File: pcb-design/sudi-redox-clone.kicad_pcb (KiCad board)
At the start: 2 copper layers, 141.8 x 99.4 mm, 143 parts, among them J1 SIDE_CON, J10 ARM_JTAG, J2 0.91 OLED, J5 SIDE_CON, J6 USB_A, J7 ARMJTAG, J8 BatCon, J9 AVR-ISP-6, K1 KEYSW, K10 KEYSW, K11 KEYSW, K12 KEYSW, K13 KEYSW, K14 KEYSW, K15 KEYSW, K16 KEYSW, K17 KEYSW, K18 KEYSW, K2 KEYSW, K3 KEYSW, K4 KEYSW, K5 KEYSW, K6 KEYSW, K7 KEYSW, K8 KEYSW, K9 KEYSW, P1 USB_C_Plug_USB2.0, SW1 RST, SW2 RCV_RST, U1 AMS1117-3.3, U2 ATmega8U2-A, U3 nRF51x22-QFxx, U4 AMS1117-3.3, U5 CH340C, U6 TP4056, U7 nRF52832-QFxx, U8 MCP23017_SS, Y3 16MHz, Y4 8MHz, Y5 32MHz

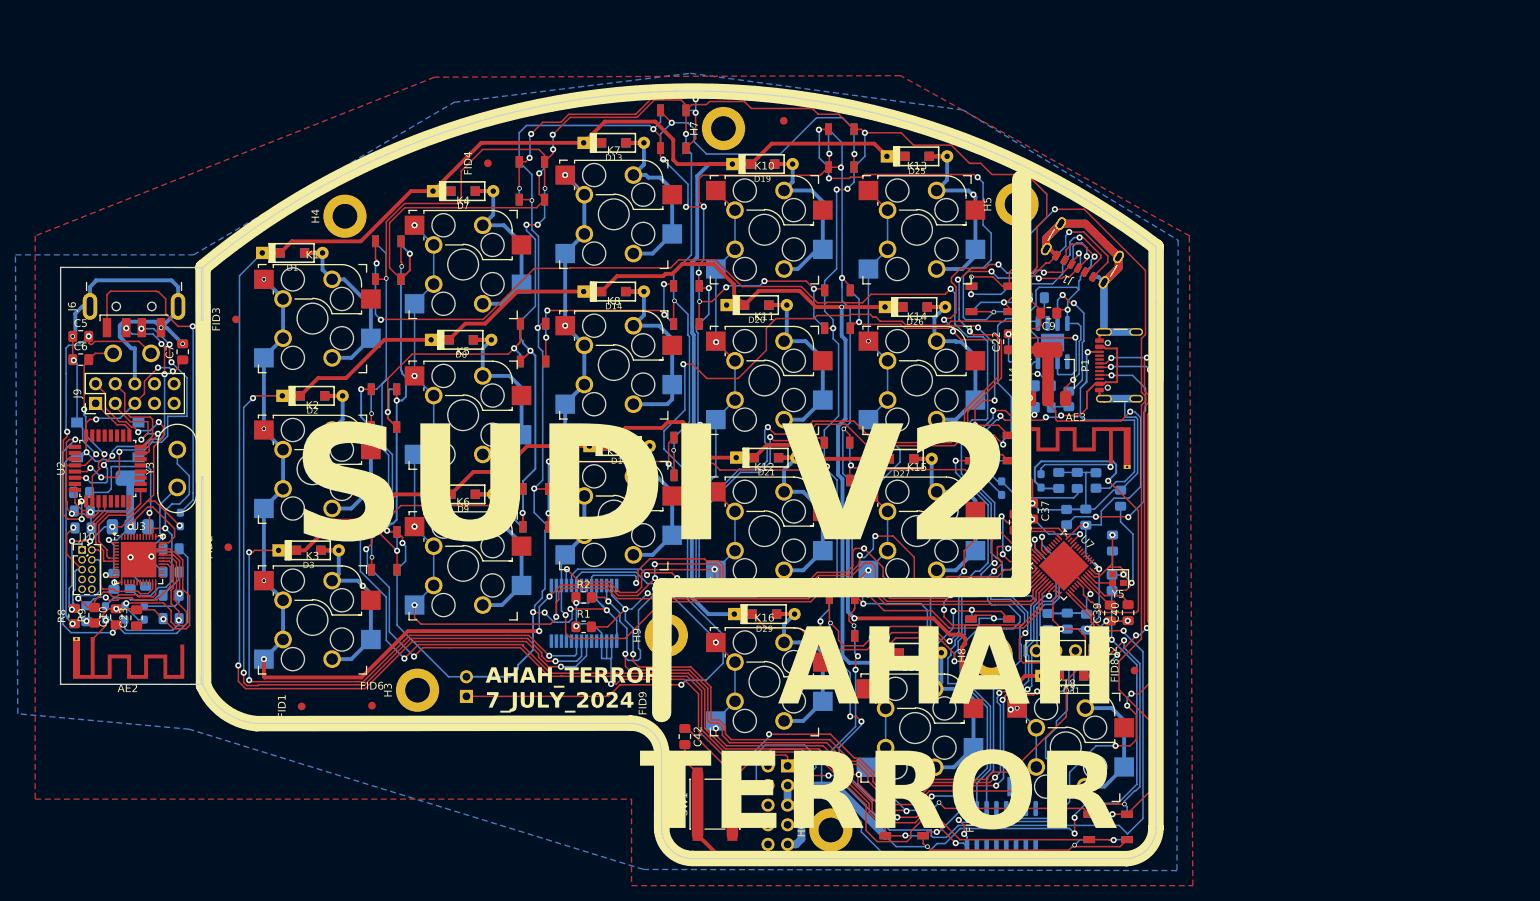
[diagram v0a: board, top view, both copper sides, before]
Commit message: [11-01-1954] add test point into NRF
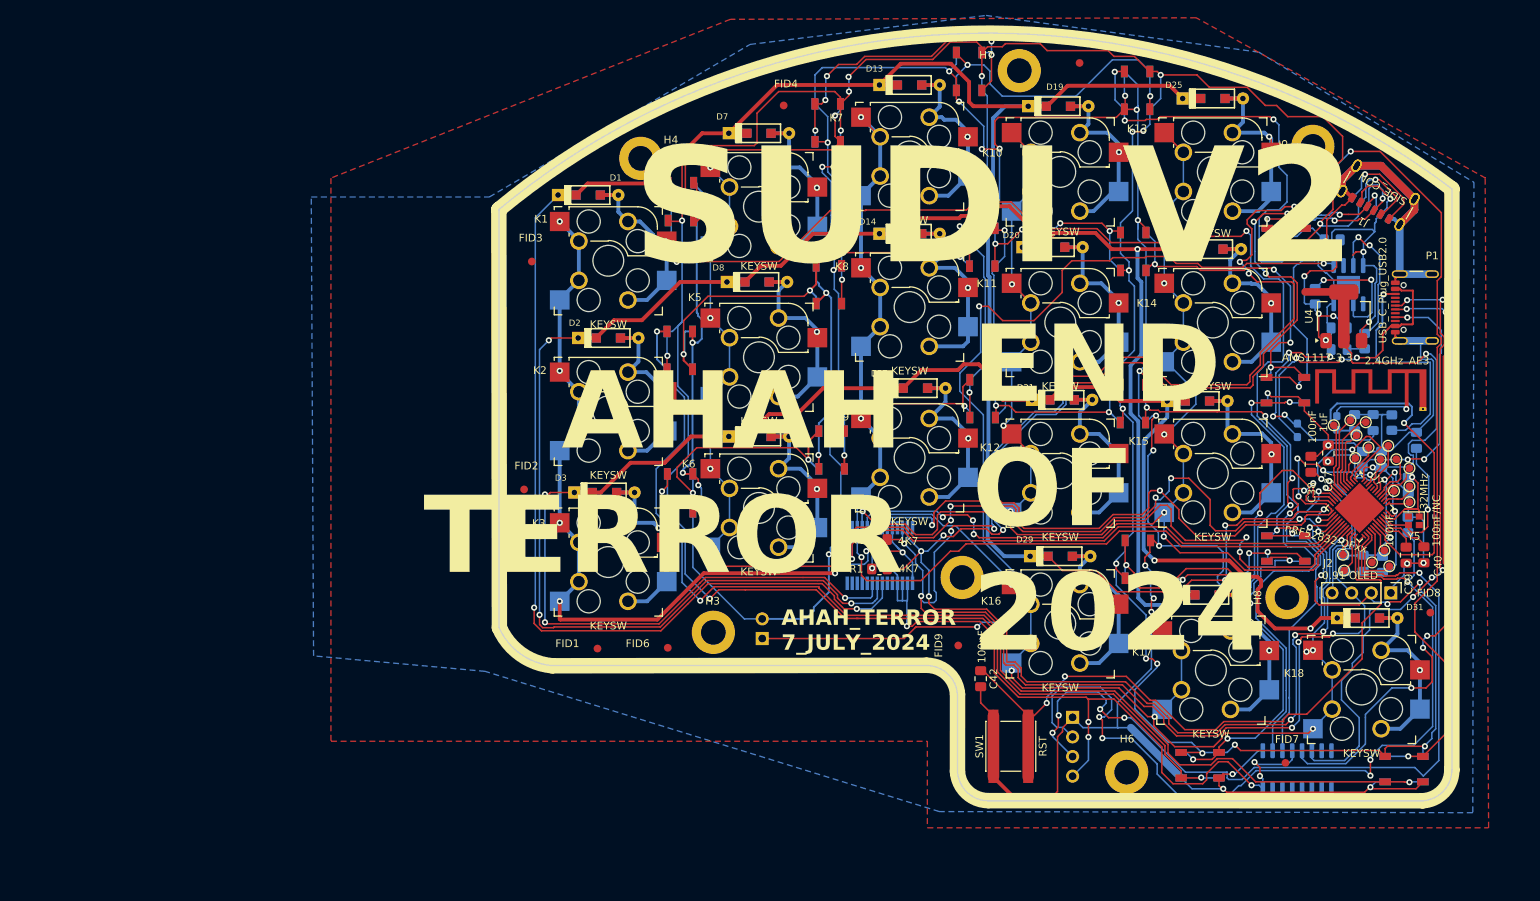
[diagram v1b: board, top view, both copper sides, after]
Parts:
- removed AE2: 2.4GHz, RF_Antenna:Texas_SWRA117D_2.4GHz_Left
- removed C10: 1uF, Capacitor_SMD:C_0805_2012Metric_Pad1.18x1.45mm_HandSolder
- removed C22, C9: 10uF/5V, Capacitor_SMD:C_0805_2012Metric_Pad1.18x1.45mm_HandSolder
- removed C23, C31, C32, C33, C7: 100nF, Capacitor_SMD:C_0805_2012Metric_Pad1.18x1.45mm_HandSolder
- removed C24: 1.5p, Capacitor_SMD:C_0805_2012Metric_Pad1.18x1.45mm_HandSolder
- removed C25: 1pF, Capacitor_SMD:C_0805_2012Metric_Pad1.18x1.45mm_HandSolder
- removed C26: 2.2pF, Capacitor_SMD:C_0805_2012Metric_Pad1.18x1.45mm_HandSolder
- removed C27: 2.2nF, Capacitor_SMD:C_0805_2012Metric_Pad1.18x1.45mm_HandSolder
- removed C28, C29: 12pF, Capacitor_SMD:C_0805_2012Metric_Pad1.18x1.45mm_HandSolder
- removed C30: 47nF, Capacitor_SMD:C_0805_2012Metric_Pad1.18x1.45mm_HandSolder
- removed C34: 1nF, Capacitor_SMD:C_0805_2012Metric_Pad1.18x1.45mm_HandSolder
- removed C5, C6: 22pF, Capacitor_SMD:C_0805_2012Metric_Pad1.18x1.45mm_HandSolder
- removed FB2: 60R@100Mhz, Inductor_SMD:L_0603_1608Metric_Pad1.05x0.95mm_HandSolder
- removed J10: ARM_JTAG, Connector_PinHeader_1.27mm:PinHeader_2x05_P1.27mm_Vertical
- removed J6: USB_A, Connector_USB:USB_A_CNCTech_1001-011-01101_Horizontal
- removed J7: ARMJTAG, Connector_PinHeader_2.54mm:PinHeader_2x05_P2.54mm_Horizontal
- removed J9: AVR-ISP-6, Connector_PinHeader_2.54mm:PinHeader_2x05_P2.54mm_Vertical
- removed L4: 3.3nH, Inductor_SMD:L_0603_1608Metric_Pad1.05x0.95mm_HandSolder
- removed L5: 10nH, Inductor_SMD:L_0603_1608Metric_Pad1.05x0.95mm_HandSolder
- removed L6: 4.7nH, Inductor_SMD:L_0603_1608Metric_Pad1.05x0.95mm_HandSolder
- removed R8, R9: 1K, Resistor_SMD:R_0805_2012Metric_Pad1.20x1.40mm_HandSolder
- removed SW2: RCV_RST, Button_Switch_SMD:SW_Push_1P1T_NO_6x6mm_H9.5mm
- removed U1: AMS1117-3.3, Package_TO_SOT_SMD:SOT-223-3_TabPin2
- removed U2: ATmega8U2-A, Package_QFP:TQFP-32_7x7mm_P0.8mm
- removed U3: nRF51x22-QFxx, Package_DFN_QFN:QFN-48-1EP_6x6mm_P0.4mm_EP4.6x4.6mm
- removed Y3: 16MHz, Crystal:Crystal_HC50_Vertical
- removed Y4: 8MHz, Crystal:Crystal_HC50_Vertical
- added J3: SWD_JLINK, Connector_PinHeader_2.54mm:PinHeader_1x04_P2.54mm_Horizontal, B.Cu at (182.7, 134.2)
- added TP1: TestPoint, TestPoint:TestPoint_Pad_D1.0mm, F.Cu at (217.7, 113.2)
- added TP10: TestPoint, TestPoint:TestPoint_Pad_D1.0mm, F.Cu at (224.6, 100.8)
- added TP11: TestPoint, TestPoint:TestPoint_Pad_D1.0mm, F.Cu at (223.5, 99.1)
- added TP12: TestPoint, TestPoint:TestPoint_Pad_D1.0mm, F.Cu at (222.5, 100.8)
- added TP14: TestPoint, TestPoint:TestPoint_Pad_D1.0mm, F.Cu at (219.3, 100.7)
- added TP15: TestPoint, TestPoint:TestPoint_Pad_D1.0mm, F.Cu at (219.4, 97.7)
- added TP17: TestPoint, TestPoint:TestPoint_Pad_D1.0mm, F.Cu at (218.6, 95.8)
- added TP18: TestPoint, TestPoint:TestPoint_Pad_D1.0mm, F.Cu at (216.5, 96.4)
- added TP2: TestPoint, TestPoint:TestPoint_Pad_D1.0mm, F.Cu at (223.7, 114.7)
- added TP3: TestPoint, TestPoint:TestPoint_Pad_D1.0mm, F.Cu at (217.8, 115.2)
- added TP4: TestPoint, TestPoint:TestPoint_Pad_D1.0mm, F.Cu at (221.4, 114.2)
- added TP5: TestPoint, TestPoint:TestPoint_Pad_D1.0mm, F.Cu at (223.0, 112.6)
- added TP6: TestPoint, TestPoint:TestPoint_Pad_D1.0mm, F.Cu at (226.3, 106.4)
- added TP7: TestPoint, TestPoint:TestPoint_Pad_D1.0mm, F.Cu at (226.3, 104.3)
- added TP8: TestPoint, TestPoint:TestPoint_Pad_D1.0mm, F.Cu at (224.3, 104.9)
- added TP9: TestPoint, TestPoint:TestPoint_Pad_D1.0mm, F.Cu at (226.3, 102.0)
- added TPe: TestPoint, TestPoint:TestPoint_Pad_D1.0mm, F.Cu at (220.6, 96.0)
- added TPe: TestPoint, TestPoint:TestPoint_Pad_D1.0mm, F.Cu at (221.0, 99.3)
- H9: moved to B.Cu
- moved C39 39.0 mm to (225.9, 113.2)
- moved FID8 39.0 mm to (229.0, 120.7)
- moved J1 39.0 mm to (222.8, 65.7)
- moved J5 39.0 mm to (222.8, 65.7)
- moved Y5 39.0 mm to (226.9, 108.8)
- moved D10 39.0 mm to (171.0, 73.4)
- moved D12 39.0 mm to (210.2, 91.9)
- moved D23 39.0 mm to (190.5, 93.6)
- moved FID7 39.0 mm to (210.2, 140.1)
- moved R6 39.0 mm to (220.5, 85.5)
- moved U6 39.0 mm to (218.4, 78.2)
- moved D5 39.0 mm to (131.8, 86.7)
- moved D13 39.0 mm to (161.6, 52.4)
- moved D14 39.0 mm to (161.6, 71.6)
- moved D15 39.0 mm to (162.3, 91.6)
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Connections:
- U7 pad 2: unconnected-(U7-P0.00/XL1-Pad2) -> /P0.00/XL1
- U7 pad 22: unconnected-(U7-P0.19-Pad22) -> /P0.19
- U7 pad 23: unconnected-(U7-P0.20-Pad23) -> /P0.20
- U7 pad 27: unconnected-(U7-P0.22-Pad27) -> /P0.22
- U7 pad 28: unconnected-(U7-P0.23-Pad28) -> /P0.23
- U7 pad 29: unconnected-(U7-P0.24-Pad29) -> /P0.24
- U7 pad 3: unconnected-(U7-P0.01/XL2-Pad3) -> /P0.01/XL2
- U7 pad 37: unconnected-(U7-P0.25-Pad37) -> /P0.25
- U7 pad 38: unconnected-(U7-P0.26-Pad38) -> /P0.26
- U7 pad 39: unconnected-(U7-P0.27-Pad39) -> /P0.27
- U7 pad 4: unconnected-(U7-P0.02/AIN0-Pad4) -> /P0.02/AIN0
- U7 pad 40: unconnected-(U7-P0.28/AIN4-Pad40) -> /P0.28/AIN4
- U7 pad 41: unconnected-(U7-P0.29/AIN5-Pad41) -> /P0.29/AIN5
- U7 pad 42: unconnected-(U7-P0.30/AIN6-Pad42) -> /P0.30/AIN6
- U7 pad 43: unconnected-(U7-P0.31/AIN7-Pad43) -> /P0.31/AIN7
- U7 pad 5: unconnected-(U7-P0.03/AIN1-Pad5) -> /P0.03/AIN1
- U7 pad 6: unconnected-(U7-P0.04/AIN2-Pad6) -> /P0.04/AIN2
- U7 pad 7: unconnected-(U7-P0.05/AIN3-Pad7) -> /P0.05/AIN3
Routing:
- net GND: track 837.4 -> 705.3 mm, vias 58 -> 47
- net /Receiver/RCV_RST: track 53.7 -> 0.00 mm, vias 5 -> 0
- net +5V: track 135.7 -> 84.9 mm, vias 14 -> 7
- net Net-(J6-VBUS): track 43.4 -> 0.00 mm, vias 1 -> 0
- net Net-(U2-XTAL1): track 41.1 -> 0.00 mm, vias 4 -> 0
- net Net-(U2-UCAP): track 37.2 -> 0.00 mm, vias 2 -> 0
- net Net-(J6-D+): track 36.5 -> 0.00 mm, vias 6 -> 0
- net Net-(J6-D-): track 34.2 -> 0.00 mm, vias 6 -> 0
- net +3.3V: track 311.0 -> 278.5 mm, vias 20 -> 16
- net Net-(U3-XC2): track 29.1 -> 0.00 mm, vias 1 -> 0
- net Net-(AE2-A): track 25.2 -> 0.00 mm, vias 1 -> 0
- net Net-(U3-ANT1): track 24.4 -> 0.00 mm, vias 1 -> 0
- net Net-(U2-PC0/XTAL2): track 24.0 -> 0.00 mm, vias 2 -> 0
- net Net-(J10-SWCLK): track 22.2 -> 0.00 mm, vias 1 -> 0
- net Net-(U3-DEC1): track 19.9 -> 0.00 mm, vias 1 -> 0
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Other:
- board size 141.8 x 99.4 mm -> 123.4 x 99.4 mm
- board text added: "9 11 2023 7 7 2024 1 11 2024"
- board text added: "END OF 2024"
- board text added: "FINISHED AT 1 NOV 2024"
- board text removed: "9 November 2023 7 Juli 2024"

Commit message: [16-11-1807] change chargin mechanism
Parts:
- removed AE3: 2.4GHz, RF_Antenna:Texas_SWRA117D_2.4GHz_Left
- removed C41: 0.8pF, Capacitor_SMD:C_0805_2012Metric_Pad1.18x1.45mm_HandSolder
- removed C42: 100nF, Capacitor_SMD:C_0805_2012Metric_Pad1.18x1.45mm_HandSolder
- removed D43, D44, D45, D46, D47, D48: WS2812B, CustomWS2185BFootPrint:LED_WS2812B_PLCC4_5.0x5.0mm_P3.2mm
- removed H8, H9: MountingHole_Pad, MountingHole:MountingHole_3.2mm_M3_DIN965_Pad
- removed J8: BatCon, Connector_PinHeader_2.54mm:PinHeader_1x02_P2.54mm_Horizontal
- removed L7: 3.9nH, Inductor_SMD:L_0603_1608Metric_Pad1.05x0.95mm_HandSolder
- removed TPe (x2): TestPoint, TestPoint:TestPoint_Pad_D1.0mm
- removed Y5: 32MHz, Crystal:Crystal_SMD_2016-4Pin_2.0x1.6mm
- added AE1: 2.4GHz, RF_Antenna:Texas_SWRA117D_2.4GHz_Left, F.Cu at (219.8, 88.7)
- added C11: 0.1uF, Capacitor_SMD:C_0805_2012Metric_Pad1.18x1.45mm_HandSolder, B.Cu at (161.3, 120.2)
- added C12: 10uF, Capacitor_SMD:C_0805_2012Metric_Pad1.18x1.45mm_HandSolder, B.Cu at (170.4, 122.2)
- added C13: 10uF, Capacitor_SMD:C_0805_2012Metric_Pad1.18x1.45mm_HandSolder, B.Cu at (170.4, 124.7)
- added C14: 10uF, Capacitor_SMD:C_0805_2012Metric_Pad1.18x1.45mm_HandSolder, B.Cu at (130.4, 125.4)
- added C15: 0.1uF, Capacitor_SMD:C_0805_2012Metric_Pad1.18x1.45mm_HandSolder, B.Cu at (130.4, 121.0)
- added C16: 10uF, Capacitor_SMD:C_0805_2012Metric_Pad1.18x1.45mm_HandSolder, B.Cu at (143.7, 116.5)
- added C17: 10uF, Capacitor_SMD:C_0805_2012Metric_Pad1.18x1.45mm_HandSolder, B.Cu at (143.7, 118.9)
- added C18: 12pF, Capacitor_SMD:C_0805_2012Metric_Pad1.18x1.45mm_HandSolder, F.Cu at (228.8, 94.5)
- added C21: 0.8pF, Capacitor_SMD:C_0805_2012Metric_Pad1.18x1.45mm_HandSolder, F.Cu at (228.1, 91.3)
- added D32: red, LED_SMD:LED_0805_2012Metric_Pad1.15x1.40mm_HandSolder, F.Cu at (149.6, 118.9)
- added D33: 1N4148, canadian_footprints:D_SOD123_axial-dual, F.Cu at (181.9, 112.8)
- added D34: 1N4148, canadian_footprints:D_SOD123_axial-dual, F.Cu at (199.8, 119.0)
- added D35: 1N4148, canadian_footprints:D_SOD123_axial-dual, F.Cu at (220.1, 139.7)
- added D36: WS2812B, LED_SMD:LED_WS2812B-2020_PLCC4_2.0x2.0mm, F.Cu at (151.5, 99.7)
- added D37: WS2812B, LED_SMD:LED_WS2812B-2020_PLCC4_2.0x2.0mm, F.Cu at (189.8, 93.2)
- added D38: WS2812B, LED_SMD:LED_WS2812B-2020_PLCC4_2.0x2.0mm, F.Cu at (228.4, 140.5)
- added H1: MountingHole_Pad, MountingHole:MountingHole_3.2mm_M3_DIN965_Pad, F.Cu at (210.6, 118.8)
- added H2: MountingHole_Pad, MountingHole:MountingHole_3.2mm_M3_DIN965_Pad, F.Cu at (169.2, 116.3)
- added J4: BatCon, Connector_PinHeader_2.54mm:PinHeader_1x02_P2.54mm_Horizontal, B.Cu at (142.4, 124.7)
- added JP1: END_TX, Jumper:SolderJumper-2_P1.3mm_Open_RoundedPad1.0x1.5mm, F.Cu at (213.6, 67.5)
- added L1: 22uH, Inductor_SMD:L_0603_1608Metric_Pad1.05x0.95mm_HandSolder, B.Cu at (166.3, 124.7)
- added L2: 22uH, Inductor_SMD:L_0603_1608Metric_Pad1.05x0.95mm_HandSolder, B.Cu at (138.8, 119.5)
- added L3: 3.9nH, Inductor_SMD:L_0603_1608Metric_Pad1.05x0.95mm_HandSolder, F.Cu at (226.3, 88.1)
- added Q1: PJA3404_(G1,D3,S2), Package_TO_SOT_SMD:SOT-23, F.Cu at (178.2, 141.6)
- added Q2: PJA3405_(G1,D3,S2), Package_TO_SOT_SMD:SOT-23, F.Cu at (218.2, 73.2)
- added R11: 1k, Resistor_SMD:R_0805_2012Metric_Pad1.20x1.40mm_HandSolder, F.Cu at (178.4, 134.9)
- added R12: 100k, Resistor_SMD:R_0805_2012Metric_Pad1.20x1.40mm_HandSolder, F.Cu at (178.4, 131.9)
- added R13: 100, Resistor_SMD:R_0805_2012Metric_Pad1.20x1.40mm_HandSolder, B.Cu at (161.3, 122.6)
- added R14: 1.13k, Resistor_SMD:R_0805_2012Metric_Pad1.20x1.40mm_HandSolder, F.Cu at (157.5, 122.8)
- added R15: 1K, Resistor_SMD:R_0805_2012Metric_Pad1.20x1.40mm_HandSolder, F.Cu at (144.8, 116.1)
- added R16: 100, Resistor_SMD:R_0805_2012Metric_Pad1.20x1.40mm_HandSolder, B.Cu at (130.5, 123.2)
- added R17: 1K, Resistor_SMD:R_0805_2012Metric_Pad1.20x1.40mm_HandSolder, F.Cu at (144.8, 118.9)
- added R5: 100k, Resistor_SMD:R_0805_2012Metric_Pad1.20x1.40mm_HandSolder, F.Cu at (178.4, 137.8)
- added SW3: PWR_SWITCH, Button_Switch_SMD:SW_SPDT_PCM12, F.Cu at (169.5, 135.7)
- added SW4: 5V_EN, Button_Switch_SMD:SW_SPDT_PCM12, B.Cu at (120.6, 126.4)
- added TP13: TestPoint, TestPoint:TestPoint_Pad_D1.0mm, F.Cu at (218.1, 92.5)
- added TP16: TestPoint, TestPoint:TestPoint_Pad_D1.0mm, F.Cu at (215.4, 96.7)
- added U9: TPS63001_SEPIC_3V3, Package_SON:Texas_DRC0010J_ThermalVias, B.Cu at (134.6, 116.9)
- added Y1: 32MHz_CF4032M00020001, Crystal:Crystal_SMD_2016-4Pin_2.0x1.6mm, F.Cu at (225.1, 96.3)
- C1: value 10uF -> 4.7uF; moved to F.Cu
- C19: value 12pF -> 100nF; moved to F.Cu
- C2, C20, C35, C8, FB1, R10, R3, R4: moved to F.Cu
- C3: value 10uF/5V -> 4.7uF; moved to F.Cu
- C36: value 100nF -> 100nF/NC; moved to F.Cu
- C40: value 100nF/NC -> 100nF
- D1, D14, D15, D2, D20, D21, D26, D27, D3, D7: value 1N5820 -> 1N4148
- D10, D12, D17, D18, D23, D24: footprint CustomWS2185BFootPrint:LED_WS2812B_PLCC4_5.0x5.0mm_P3.2mm -> LED_SMD:LED_WS2812B-2020_PLCC4_2.0x2.0mm; moved to F.Cu
- D11: footprint CustomWS2185BFootPrint:LED_WS2812B_PLCC4_5.0x5.0mm_P3.2mm -> LED_SMD:LED_WS2812B-2020_PLCC4_2.0x2.0mm
- D13, D19, D25, D29, D30, D31, D8, D9: value 1N5820 -> WS2812B; footprint canadian_footprints:D_SOD123_axial-dual -> LED_SMD:LED_WS2812B-2020_PLCC4_2.0x2.0mm
- D16, D5: value WS2812B -> 1N4148; footprint CustomWS2185BFootPrint:LED_WS2812B_PLCC4_5.0x5.0mm_P3.2mm -> canadian_footprints:D_SOD123_axial-dual; moved to F.Cu
- D22, D28, D6: value WS2812B -> 1N4148; footprint CustomWS2185BFootPrint:LED_WS2812B_PLCC4_5.0x5.0mm_P3.2mm -> canadian_footprints:D_SOD123_axial-dual
- D4: value RED -> green; moved to F.Cu
- J2: value 0.91 OLED -> SWD_JLINK; footprint Connector_PinHeader_2.54mm:PinHeader_1x04_P2.54mm_Vertical -> Connector_PinHeader_2.54mm:PinHeader_1x04_P2.54mm_Horizontal; moved to B.Cu
- J3: value SWD_JLINK -> 0.91 OLED; footprint Connector_PinHeader_2.54mm:PinHeader_1x04_P2.54mm_Horizontal -> Connector_PinHeader_2.54mm:PinHeader_1x04_P2.54mm_Vertical; moved to F.Cu
- R6: value 1K -> 46.4K; moved to F.Cu
- R7: value 1.2 -> 1.18k; moved to F.Cu
- SW1: moved to B.Cu
- U4: value AMS1117-3.3 -> CH340C; footprint Package_TO_SOT_SMD:SOT-223-3_TabPin2 -> Package_SO:SOIC-16_3.9x9.9mm_P1.27mm; moved to B.Cu
- U5: value CH340C -> BQ24075RGT_DPPM; footprint Package_SO:SOIC-16_3.9x9.9mm_P1.27mm -> Package_DFN_QFN:VQFN-16-1EP_3x3mm_P0.5mm_EP1.6x1.6mm; moved to F.Cu
- U6: value TP4056 -> TPS63002_SEPIC_5V; footprint Package_SO:SOIC-8-1EP_3.9x4.9mm_P1.27mm_EP2.29x3mm -> Package_SON:Texas_DRC0010J_ThermalVias
- moved D25 78.1 mm to (189.5, 131.4), turned to 90 degrees
- moved C3 76.6 mm to (149.2, 122.4), turned to 180 degrees
- moved C4 76.1 mm to (161.3, 125.0)
- moved R6 75.1 mm to (155.3, 122.8)
- moved R7 74.7 mm to (153.1, 122.8), turned to -90 degrees
- moved D4 73.8 mm to (149.5, 116.1)
- moved C1 70.3 mm to (153.4, 113.4), turned to 180 degrees
- moved U6 67.7 mm to (166.2, 121.4)
- moved D16 62.8 mm to (161.2, 90.5), turned to 0 degrees
- moved U5 62.1 mm to (154.3, 117.5)
- moved D24 60.7 mm to (190.5, 55.0), turned to 90 degrees
- moved D11 59.8 mm to (132.2, 87.0), turned to 90 degrees
- moved D13 53.1 mm to (210.2, 73.8), turned to 90 degrees
- moved D9 52.3 mm to (170.7, 54.1), turned to 90 degrees
- moved D23 52.2 mm to (151.2, 59.2), turned to 90 degrees
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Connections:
- net Tx renamed END_TX
- C1 pad 1: +5V -> +BATT
- C19 pad 1: GND -> Net-(U7-P0.21/~{RESET})
- C19 pad 2: Net-(U7-XC2) -> GND
- C2 pad 1: +5V -> VBUS
- C20 pad 1: +3.3V -> GND
- C20 pad 2: GND -> Net-(U7-DEC1)
- C3 pad 1: +3.3V -> VDD
- C35 pad 1: +3.3V -> GND
- C35 pad 2: GND -> Net-(U7-DEC2)
- C36 pad 1: +3.3V -> GND
- C36 pad 2: GND -> Net-(U7-DEC3)
- C38 pad 1: GND -> +3.3V
- C38 pad 2: Net-(U7-DEC1) -> GND
- C39 pad 1: GND -> +3.3V
- C39 pad 2: Net-(U7-DEC2) -> GND
- C4 pad 1: Net-(J8-Pin_1) -> VDD
- C40 pad 1: GND -> +3.3V
- C40 pad 2: Net-(U7-DEC3) -> GND
- D10 pad 1: +3V7 -> Net-(D10-DOUT)
- D10 pad 2: Net-(D10-DOUT) -> GND
- D10 pad 3: GND -> /DOUT2
- D10 pad 4: Net-(D10-DIN) -> +5V
- D11 pad 1: +3V7 -> Net-(D11-DOUT)
- D11 pad 2: Net-(D11-DOUT) -> GND
- D11 pad 3: GND -> Net-(D11-DIN)
- D11 pad 4: Net-(D10-DOUT) -> +5V
- D12 pad 1: +3V7 -> Net-(D12-DOUT)
- D12 pad 2: Net-(D12-DOUT) -> GND
- D12 pad 3: GND -> Net-(D12-DIN)
- D12 pad 4: Net-(D11-DOUT) -> +5V
- D13 pad 1: row1 -> Net-(D13-DOUT)
- D13 pad 2: Net-(D13-A) -> GND
- D14 pad 1: row2 -> row1
- D15 pad 1: row3 -> row2
- D16 pad 1: +3V7 -> row3
- D16 pad 2: Net-(D16-DOUT) -> Net-(D16-A)
- D17 pad 1: +3V7 -> Net-(D17-DOUT)
- D17 pad 2: Net-(D17-DOUT) -> GND
- D17 pad 3: GND -> Net-(D11-DOUT)
- D17 pad 4: Net-(D16-DOUT) -> +5V
- D18 pad 1: +3V7 -> Net-(D18-DOUT)
- D18 pad 2: Net-(D18-DOUT) -> GND
- D18 pad 3: GND -> Net-(D12-DOUT)
- D18 pad 4: Net-(D17-DOUT) -> +5V
- D19 pad 1: row1 -> Net-(D19-DOUT)
- D19 pad 2: Net-(D19-A) -> GND
- D20 pad 1: row2 -> row1
- D21 pad 1: row3 -> row2
- D22 pad 1: +3V7 -> row3
- D22 pad 2: Net-(D22-DOUT) -> Net-(D22-A)
- D23 pad 1: +3V7 -> Net-(D23-DOUT)
- D23 pad 2: Net-(D23-DOUT) -> GND
- D23 pad 3: GND -> Net-(D17-DOUT)
- D23 pad 4: Net-(D22-DOUT) -> +5V
- D24 pad 1: +3V7 -> Net-(D24-DOUT)
- D24 pad 2: Net-(D24-DOUT) -> GND
- D24 pad 3: GND -> Net-(D18-DOUT)
- D24 pad 4: Net-(D23-DOUT) -> +5V
- D25 pad 1: row1 -> Net-(D25-DOUT)
- D25 pad 2: Net-(D25-A) -> GND
- D26 pad 1: row2 -> row1
- D27 pad 1: row3 -> row2
- D28 pad 1: +3V7 -> row3
- D28 pad 2: unconnected-(D28-DOUT-Pad2) -> Net-(D28-A)
- D29 pad 1: row1 -> Net-(D29-DOUT)
- D29 pad 2: Net-(D29-A) -> GND
- D30 pad 1: row2 -> Net-(D30-DOUT)
- D30 pad 2: Net-(D30-A) -> GND
- D31 pad 1: row3 -> Net-(D31-DOUT)
- D31 pad 2: Net-(D31-A) -> GND
- D4 pad 2: +5V -> Net-(D4-A)
- D5 pad 1: +3V7 -> row1
- D5 pad 2: Net-(D5-DOUT) -> Net-(D5-A)
- D6 pad 1: +3V7 -> row2
- D6 pad 2: Net-(D10-DIN) -> Net-(D6-A)
- D7 pad 1: row1 -> row3
- D8 pad 1: row2 -> Net-(D11-DIN)
- D8 pad 2: Net-(D8-A) -> GND
- D9 pad 1: row3 -> Net-(D12-DIN)
- D9 pad 2: Net-(D9-A) -> GND
- FB1 pad 1: Net-(FB1-Pad1) -> Net-(Q2-S)
- FB1 pad 2: +5V -> VBUS
- J1 pad B9: +3V7 -> +3.3V
- J2 pad 2: +3V7 -> /SWCLK
- J2 pad 3: SCL -> /SWDIO
- J2 pad 4: SDA -> +3.3V
- J3 pad 2: /SWCLK -> +3.3V
- J3 pad 3: /SWDIO -> SCL
- J3 pad 4: +3.3V -> SDA
- J5 pad B9: +3V7 -> +3.3V
- K10 pad 2: Net-(D19-A) -> Net-(D20-A)
- K11 pad 2: Net-(D20-A) -> Net-(D21-A)
- K12 pad 2: Net-(D21-A) -> Net-(D22-A)
- K13 pad 2: Net-(D25-A) -> Net-(D26-A)
- K14 pad 2: Net-(D26-A) -> Net-(D27-A)
- K15 pad 2: Net-(D27-A) -> Net-(D28-A)
- K16 pad 2: Net-(D29-A) -> Net-(D33-A)
- K17 pad 2: Net-(D30-A) -> Net-(D34-A)
- K18 pad 2: Net-(D31-A) -> Net-(D35-A)
- K4 pad 2: Net-(D7-A) -> Net-(D5-A)
- K5 pad 2: Net-(D8-A) -> Net-(D6-A)
- K6 pad 2: Net-(D9-A) -> Net-(D7-A)
- K7 pad 2: Net-(D13-A) -> Net-(D14-A)
- K8 pad 2: Net-(D14-A) -> Net-(D15-A)
- K9 pad 2: Net-(D15-A) -> Net-(D16-A)
- P1 pad A4: Net-(FB1-Pad1) -> Net-(Q2-D)
- P1 pad A9: Net-(FB1-Pad1) -> Net-(Q2-D)
- P1 pad B4: Net-(FB1-Pad1) -> Net-(Q2-D)
- P1 pad B9: Net-(FB1-Pad1) -> Net-(Q2-D)
- R6 pad 1: Net-(U6-~{CHRG}) -> /TMR
- R6 pad 2: Net-(D4-K) -> GND
- R7 pad 1: GND -> /ILIM
- R7 pad 2: Net-(U6-PROG) -> GND
- TP1 pad 1: /P0.19 -> /P0.00/XL1
- TP10 pad 1: /P0.29/AIN5 -> /P0.23
- TP11 pad 1: /P0.30/AIN6 -> /P0.24
- TP12 pad 1: /P0.31/AIN7 -> /P0.25
- TP14 pad 1: /P0.01/XL2 -> /P0.27
- TP15 pad 1: /P0.02/AIN0 -> /P0.28/AIN4
- TP17 pad 1: /P0.04/AIN2 -> /P0.30/AIN6
- TP18 pad 1: /P0.05/AIN3 -> /P0.31/AIN7
- TP2 pad 1: /P0.22 -> /P0.01/XL2
- TP3 pad 1: /P0.20 -> /P0.02/AIN0
- TP4 pad 1: /P0.23 -> /P0.03/AIN1
- TP5 pad 1: /P0.24 -> /P0.04/AIN2
- TP6 pad 1: /P0.25 -> /P0.05/AIN3
- TP7 pad 1: /P0.26 -> /P0.19
- TP8 pad 1: /P0.27 -> /P0.20
- TP9 pad 1: /P0.28/AIN4 -> /P0.22
- U4 pad 2: +3.3V -> RX
- U4 pad 3: +5V -> TX
- U5 pad 1: GND -> unconnected-(U5-TS-Pad1)
- U5 pad 10: unconnected-(U5-~{DSR}-Pad10) -> VDD
- U5 pad 11: unconnected-(U5-~{RI}-Pad11) -> VDD
- U5 pad 12: unconnected-(U5-~{DCD}-Pad12) -> /ILIM
- U5 pad 13: unconnected-(U5-~{DTR}-Pad13) -> VBUS
- U5 pad 14: unconnected-(U5-~{RTS}-Pad14) -> /TMR
- U5 pad 15: unconnected-(U5-R232-Pad15) -> /SYSOFF
- U5 pad 16: +3.3V -> /ISET
- U5 pad 2: RX -> +BATT
- U5 pad 3: TX -> +BATT
- U5 pad 4: +3.3V -> GND
- U5 pad 5: Net-(P1-D+) -> VDD
- U5 pad 6: Net-(P1-D-) -> GND
- U5 pad 7: unconnected-(U5-NC-Pad7) -> Net-(D4-K)
- U5 pad 8: unconnected-(U5-~{OUT}/~{DTR}-Pad8) -> GND
- U5 pad 9: unconnected-(U5-~{CTS}-Pad9) -> Net-(D32-K)
- U6 pad 1: unconnected-(U6-TEMP-Pad1) -> +5V
- U6 pad 2: Net-(U6-PROG) -> Net-(U6-L2)
- U6 pad 4: +5V -> Net-(U6-L1)
- U6 pad 5: Net-(J8-Pin_1) -> VDD
- U6 pad 6: unconnected-(U6-~{STDBY}-Pad6) -> Net-(SW4-B)
- U6 pad 7: Net-(U6-~{CHRG}) -> Net-(SW4-A)
- U6 pad 8: +5V -> Net-(SW4-A)
- U6 pad 9: unconnected-(U6-PP-Pad9) -> GND
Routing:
- net +3V7: track 539.7 -> 0.00 mm, vias 32 -> 0
- net +5V: track 84.9 -> 558.7 mm, vias 7 -> 26
- net VBUS: track 0.00 -> 183.0 mm, vias 0 -> 5
- net Net-(D48-DOUT): track 150.7 -> 0.00 mm, vias 3 -> 0
- net +3.3V: track 278.5 -> 140.8 mm, vias 16 -> 13
- net Net-(J8-Pin_1): track 134.6 -> 0.00 mm, vias 3 -> 0
- net Net-(D47-DOUT): track 114.3 -> 0.00 mm, vias 4 -> 0
- net END_TX: track 13.5 -> 116.9 mm, vias 1 -> 7
- net Net-(D16-DOUT): track 99.9 -> 0.00 mm, vias 3 -> 0
- net row1: track 322.3 -> 231.4 mm
- net SCL: track 244.4 -> 156.3 mm, vias 14 -> 8
- net /DOUT1: track 0.00 -> 72.8 mm, vias 0 -> 3
- net Net-(P1-D-): track 81.8 -> 11.3 mm, vias 5 -> 1
- net Net-(P1-D+): track 82.4 -> 13.3 mm, vias 5 -> 1
- net +BATT: track 0.00 -> 67.2 mm, vias 0 -> 2
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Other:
- board text added: "FINISHED AT 16 NOV 2024"
- board text removed: "FINISHED AT 1 NOV 2024"
